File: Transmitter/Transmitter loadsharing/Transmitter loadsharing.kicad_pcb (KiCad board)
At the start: 4 copper layers, 57 x 80.5 mm, 65 parts, among them J1 Conn_Coaxial, J2 Conn_01x01, J3 Conn_01x03, J4 Conn_01x02_Socket, J5 Conn_01x02, J6 Conn_01x02, J7 Conn_01x02, J8 Conn_01x02_Socket, U1 OPA3692IDBQR, U2 THS3091D, U3 THS3091D, U4 THS3091D, U5 THS3091D, U6 THS3091D, U7 THS3091D

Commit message: First revision of Tx board
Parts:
- added C26: 0.47u, Capacitor_SMD:C_0603_1608Metric_Pad1.08x0.95mm_HandSolder, F.Cu at (177.8, 105.8)
- added C27: 10u, Capacitor_SMD:C_0603_1608Metric_Pad1.08x0.95mm_HandSolder, F.Cu at (172.1, 103.4)
- added C28: 10u, Capacitor_SMD:C_0603_1608Metric_Pad1.08x0.95mm_HandSolder, F.Cu at (184.1, 103.3)
- added C29: 22u, Capacitor_SMD:C_0603_1608Metric_Pad1.08x0.95mm_HandSolder, F.Cu at (207.4, 116.7)
- added C30: 0.47u, Capacitor_SMD:C_0603_1608Metric_Pad1.08x0.95mm_HandSolder, F.Cu at (207.2, 105.8)
- added C31: 10u, Capacitor_SMD:C_0603_1608Metric_Pad1.08x0.95mm_HandSolder, F.Cu at (201.3, 103.4)
- added C32: 10u, Capacitor_SMD:C_0603_1608Metric_Pad1.08x0.95mm_HandSolder, F.Cu at (213.3, 103.4)
- added C9: 10u, Capacitor_SMD:C_0603_1608Metric_Pad1.08x0.95mm_HandSolder, F.Cu at (178.1, 116.7)
- added D2: LED, LED_SMD:LED_0603_1608Metric_Pad1.05x0.95mm_HandSolder, F.Cu at (202.2, 90.5)
- added J10: Conn_01x01, Connector_PinHeader_2.54mm:PinHeader_1x01_P2.54mm_Vertical, F.Cu at (120.8, 92.9)
- added J11: Conn_01x01, Connector_PinHeader_2.54mm:PinHeader_1x01_P2.54mm_Vertical, F.Cu at (167.8, 120.4)
- added J12: Conn_01x01, Connector_PinHeader_2.54mm:PinHeader_1x01_P2.54mm_Vertical, F.Cu at (171.7, 97.0)
- added J13: Conn_01x01, Connector_PinHeader_2.54mm:PinHeader_1x01_P2.54mm_Vertical, F.Cu at (219.0, 120.3)
- added J14: Conn_01x01, Connector_PinHeader_2.54mm:PinHeader_1x01_P2.54mm_Vertical, F.Cu at (197.2, 97.0)
- added J15: Conn_01x01, Connector_PinHeader_2.54mm:PinHeader_1x01_P2.54mm_Vertical, F.Cu at (97.5, 127.5)
- added J16: Conn_01x01, Connector_PinHeader_2.54mm:PinHeader_1x01_P2.54mm_Vertical, F.Cu at (113.2, 131.2)
- added J17: Conn_Coaxial, Connector_Coaxial:BNC_Amphenol_B6252HB-NPP3G-50_Horizontal, F.Cu at (179.0, 125.3)
- added J18: Conn_Coaxial, Connector_Coaxial:BNC_Amphenol_B6252HB-NPP3G-50_Horizontal, F.Cu at (208.2, 125.5)
- added J19: Conn_Coaxial, 132289 SMA:CONN_132289_AMP, F.Cu at (88.8, 121.6)
- added J20: Conn_01x01, Connector_PinHeader_2.54mm:PinHeader_1x01_P2.54mm_Vertical, F.Cu at (179.0, 120.4)
- added J21: Conn_01x01, Connector_PinHeader_2.54mm:PinHeader_1x01_P2.54mm_Vertical, F.Cu at (208.2, 120.4)
- added J22: Conn_01x01, Connector_PinHeader_2.54mm:PinHeader_1x01_P2.54mm_Vertical, F.Cu at (99.8, 118.5)
- added J23: Conn_01x01, Connector_PinHeader_2.54mm:PinHeader_1x01_P2.54mm_Vertical, F.Cu at (110.2, 122.7)
- added J9: Conn_01x01, Connector_PinHeader_2.54mm:PinHeader_1x01_P2.54mm_Vertical, F.Cu at (120.8, 121.7)
- added R23: R, Resistor_SMD:R_0603_1608Metric_Pad0.98x0.95mm_HandSolder, F.Cu at (197.5, 90.5)
- added R24: 50 Ohm, Resistor_SMD:R_0603_1608Metric_Pad0.98x0.95mm_HandSolder, F.Cu at (102.3, 129.8)
- added R25: 50 Ohm, Resistor_SMD:R_0603_1608Metric_Pad0.98x0.95mm_HandSolder, F.Cu at (104.3, 127.0)
- added R26: 50 Ohm, Resistor_SMD:R_0603_1608Metric_Pad0.98x0.95mm_HandSolder, F.Cu at (106.1, 129.8)
- added R28: 0 Ohm, Resistor_SMD:R_0603_1608Metric_Pad0.98x0.95mm_HandSolder, F.Cu at (96.7, 112.3)
- added R29: R, Resistor_SMD:R_0603_1608Metric_Pad0.98x0.95mm_HandSolder, F.Cu at (99.2, 111.4)
- added R30: 0 Ohm, Resistor_SMD:R_0603_1608Metric_Pad0.98x0.95mm_HandSolder, F.Cu at (109.2, 112.3)
- added R31: R, Resistor_SMD:R_0603_1608Metric_Pad0.98x0.95mm_HandSolder, F.Cu at (112.0, 111.4)
- added R32: 0 Ohm, Resistor_SMD:R_0603_1608Metric_Pad0.98x0.95mm_HandSolder, F.Cu at (121.8, 112.3)
- added R33: R, Resistor_SMD:R_0603_1608Metric_Pad0.98x0.95mm_HandSolder, F.Cu at (124.5, 111.4)
- added R34: 0 Ohm, Resistor_SMD:R_0603_1608Metric_Pad0.98x0.95mm_HandSolder, F.Cu at (147.8, 112.3)
- added R35: R, Resistor_SMD:R_0603_1608Metric_Pad0.98x0.95mm_HandSolder, F.Cu at (150.7, 111.4)
- added R36: 0 Ohm, Resistor_SMD:R_0603_1608Metric_Pad0.98x0.95mm_HandSolder, F.Cu at (161.0, 112.3)
- added R37: R, Resistor_SMD:R_0603_1608Metric_Pad0.98x0.95mm_HandSolder, F.Cu at (163.8, 111.4)
- added R38: 0 Ohm, Resistor_SMD:R_0603_1608Metric_Pad0.98x0.95mm_HandSolder, F.Cu at (134.6, 112.3)
- added R39: R, Resistor_SMD:R_0603_1608Metric_Pad0.98x0.95mm_HandSolder, F.Cu at (137.4, 111.4)
- added R40: 24.9k, Resistor_SMD:R_0603_1608Metric_Pad0.98x0.95mm_HandSolder, F.Cu at (179.7, 105.9)
- added R41: 24.9k, Resistor_SMD:R_0603_1608Metric_Pad0.98x0.95mm_HandSolder, F.Cu at (209.4, 105.9)
- added U10: LT3094EMSE-PBF, LT3094:05-08-1666_ADI, F.Cu at (202.3, 108.6)
- added U11: LT3094EMSE-PBF, LT3094:05-08-1666_ADI, F.Cu at (214.3, 108.6)
- added U8: LT3045EMSE-PBF, LT3045:MSOP12_MSE_ADI, F.Cu at (185.1, 108.6)
- added U9: LT3045EMSE-PBF, LT3045:MSOP12_MSE_ADI, F.Cu at (173.1, 108.6)
- C1, C10, C11, C12, C13, C14, C15, C16, C17, C18, C19, C2, C20, C21, C22, C23, C24, C25, C3, C4, C5, C6, C7: footprint Capacitor_SMD:C_0805_2012Metric_Pad1.18x1.45mm_HandSolder -> Capacitor_SMD:C_0603_1608Metric_Pad1.08x0.95mm_HandSolder
- D1: footprint LED_SMD:LED_0805_2012Metric_Pad1.15x1.40mm_HandSolder -> LED_SMD:LED_0603_1608Metric_Pad1.05x0.95mm_HandSolder
- J1: footprint Amphenol 112404:CONN_112404_AMP -> 132289 SMA:CONN_132289_AMP
- J2: value Conn_01x01 -> Conn_01x03; footprint Connector_PinHeader_2.54mm:PinHeader_1x01_P2.54mm_Vertical -> Connector_PinHeader_2.54mm:PinHeader_1x03_P2.54mm_Vertical
- J6: value Conn_01x02 -> Conn_01x01; footprint Connector_PinHeader_2.54mm:PinHeader_1x02_P2.54mm_Vertical -> Connector_PinHeader_2.54mm:PinHeader_1x01_P2.54mm_Vertical
- R1, R10, R11, R12, R13, R14, R15, R16, R17, R18, R19, R2, R20, R21, R22, R3, R4, R5, R6, R7, R8, R9: footprint Resistor_SMD:R_0805_2012Metric_Pad1.20x1.40mm_HandSolder -> Resistor_SMD:R_0603_1608Metric_Pad0.98x0.95mm_HandSolder
- U1: footprint Opa3962:DBQ16 -> Opa3692 SOIC:DBQ16
- moved R3 113.6 mm to (90.9, 110.1), turned to 0 degrees
- moved C15 112.7 mm to (92.7, 101.4), turned to 0 degrees
- moved R2 112.6 mm to (91.9, 106.8), turned to -90 degrees
- moved C14 110.0 mm to (103.8, 113.2), turned to 0 degrees
- moved R4 107.4 mm to (96.7, 100.7), turned to 90 degrees
- moved U2 106.9 mm to (96.0, 106.5), turned to 90 degrees
- moved C11 100.7 mm to (100.2, 108.3), turned to 90 degrees
- moved C10 99.4 mm to (103.8, 98.0), turned to 0 degrees
- moved R5 95.4 mm to (103.9, 110.1), turned to 0 degrees
- moved R6 94.6 mm to (104.8, 106.8), turned to -90 degrees
- moved C13 94.5 mm to (105.8, 101.4), turned to 0 degrees
- moved R7 89.7 mm to (109.5, 100.7), turned to 90 degrees
- moved U3 89.3 mm to (108.6, 106.5), turned to 90 degrees
- moved J1 89.3 mm to (104.1, 136.2)
- moved R11 87.3 mm to (109.2, 116.0), turned to 90 degrees
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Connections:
- C1 pad 1: Net-(J1-In) -> Net-(J23-Pin_1)
- J1 pad 1: Net-(J1-In) -> /Signal in
- J2 pad 1: GND -> /+5V_In
- J3 pad 1: -5V -> /-5V_In
- J3 pad 2: GND -> -5V
- J3 pad 3: +5V -> /PWR-
- U2 pad 3: /loadshare input + -> Net-(U2-VIN+)
- U3 pad 3: /loadshare input + -> Net-(U3-VIN+)
- U4 pad 3: /loadshare input + -> Net-(U4-VIN+)
- U5 pad 3: /loadshare input - -> Net-(U5-VIN+)
- U6 pad 3: /loadshare input - -> Net-(U6-VIN+)
- U7 pad 3: /loadshare input - -> Net-(U7-VIN+)
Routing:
- net /PWR+: track 0.00 -> 69.3 mm, vias 0 -> 4
- net /PWR-: track 0.00 -> 63.1 mm
- net /+5V_In: track 0.00 -> 30.2 mm
- net /-5V_In: track 0.00 -> 30.2 mm
- net Net-(J23-Pin_1): track 0.00 -> 28.7 mm
- net -5V: track 22.7 -> 48.0 mm, vias 10 -> 12
- net /Ref out: track 0.00 -> 21.8 mm
- net Net-(U10-SET): track 0.00 -> 14.6 mm, vias 0 -> 2
- net Net-(U8-SET): track 0.00 -> 14.5 mm, vias 0 -> 2
- net Net-(J1-In): track 9.56 -> 0.00 mm
- net /loadshare input +: track 37.9 -> 28.5 mm
- net /loadshare input -: track 39.1 -> 29.9 mm
- net /Signal in: track 0.00 -> 8.26 mm
- net Net-(U6-VIN+): track 0.00 -> 4.37 mm
- net Net-(U4-VIN+): track 0.00 -> 4.34 mm
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- added copper zone on In2.Cu, net -5V
- added copper zone on B.Cu, net GND
- added copper zone on F.Cu, net GND
- removed copper zone on B.Cu, net -5V
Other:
- board size 57 x 80.5 mm -> 145 x 50.8 mm
- board text added: "+PWR input"
- board text added: "+Power select"
- board text added: "-PWR input"
- board text added: "-Power select"
- board text added: "PWR+"
- board text added: "PWR-"
- board text added: "Ref"
- board text added: "Ref Out"
- board text added: "Signal In"
- board text added: "Transmitter 1.1 2024-04-19"
- board text removed: "Transmitter 1.0 2024-04-19"

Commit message: Small corrections, changed footprint for edge SMA connectors
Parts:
- J1, J19: footprint 132289 SMA:CONN_132289_AMP -> Connector_Coaxial:SMA_Amphenol_132289_EdgeMount
- moved J1 0.95 mm to (104.2, 135.2), turned to -90 degrees
- moved J19 0.91 mm to (89.8, 121.6), turned to 180 degrees

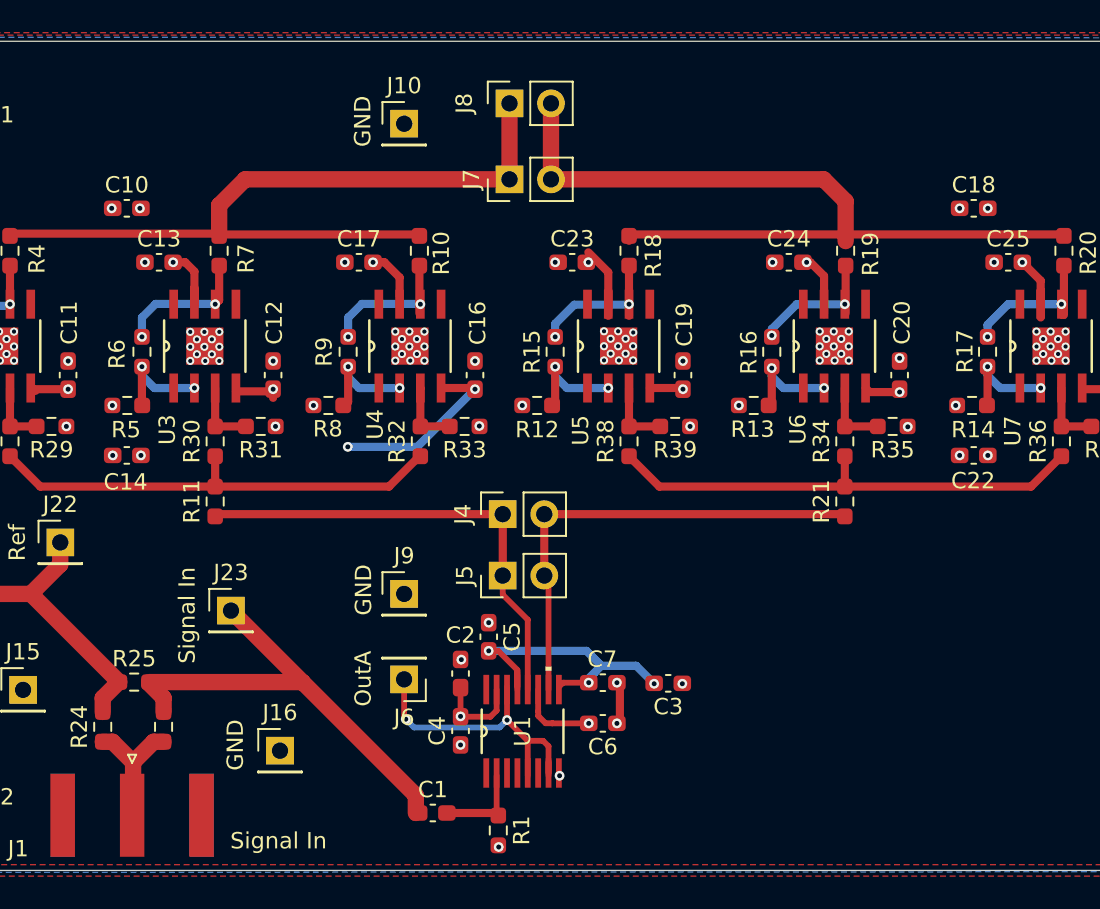
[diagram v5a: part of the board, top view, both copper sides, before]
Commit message: Added test point after HPF and§ capactitors for coil tuning
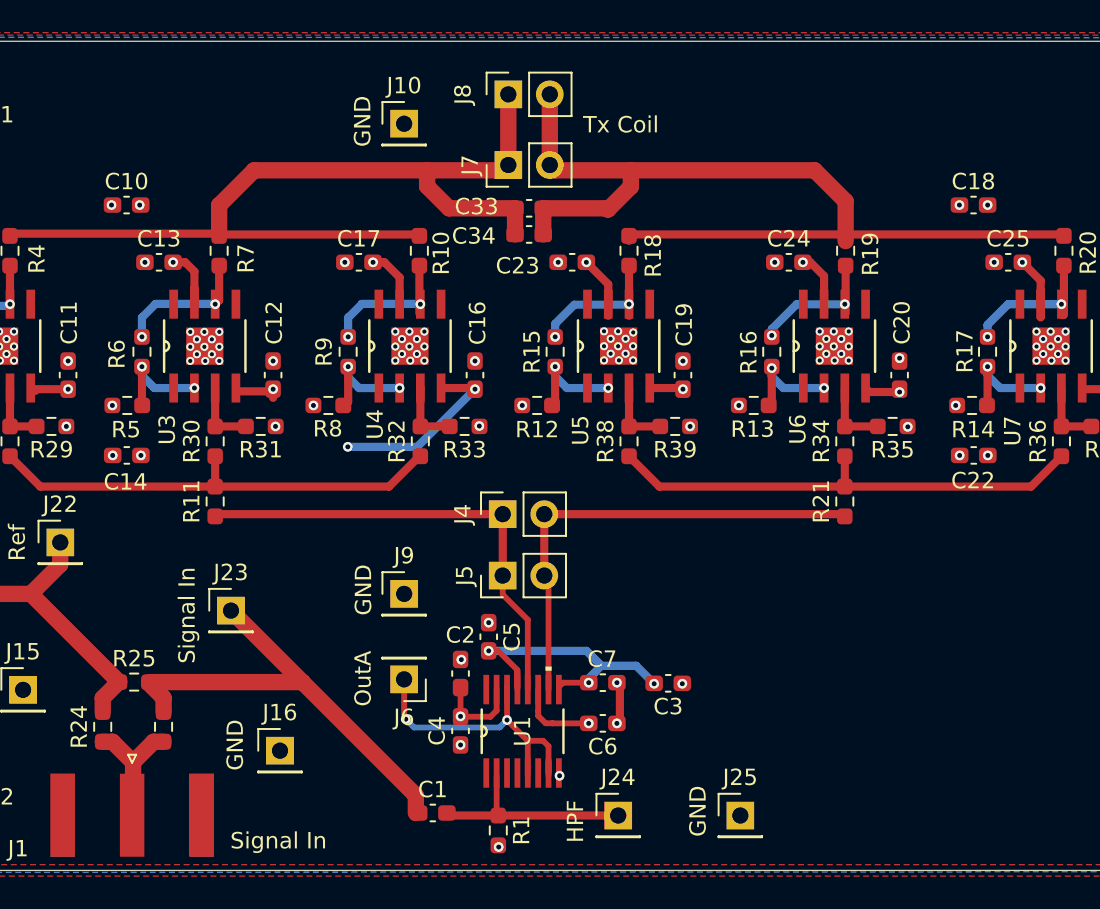
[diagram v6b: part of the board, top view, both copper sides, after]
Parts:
- added C33: C, Capacitor_SMD:C_0603_1608Metric_Pad1.08x0.95mm_HandSolder, F.Cu at (128.4, 98.0)
- added C34: C, Capacitor_SMD:C_0603_1608Metric_Pad1.08x0.95mm_HandSolder, F.Cu at (128.4, 99.7)
- added J24: Conn_01x01, Connector_PinHeader_2.54mm:PinHeader_1x01_P2.54mm_Vertical, F.Cu at (133.9, 135.2)
- added J25: Conn_01x01, Connector_PinHeader_2.54mm:PinHeader_1x01_P2.54mm_Vertical, F.Cu at (141.4, 135.2)
- moved J7 0.88 mm to (127.2, 95.4)
- moved J8 0.56 mm to (127.2, 91.1)
- moved C10 0.20 mm to (103.8, 97.8)
- moved C18 0.20 mm to (155.7, 97.8)
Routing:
- net /coil load end: track 53.2 -> 61.9 mm
- net /coil load start: track 49.9 -> 58.6 mm
- net Net-(J24-Pin_1): track 5.39 -> 12.7 mm
- net +5V: track 43.3 -> 42.7 mm
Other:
- board text added: "HPF"
- board text added: "Tx Coil"
